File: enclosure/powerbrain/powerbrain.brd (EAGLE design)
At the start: 27.3 x 64.8 mm, 38 parts, among them J2 USB-A-S, J3 AVR_SPI_PRG_6PTH, Q2 200mA/50V, X2 ZX62D-B-5PA8

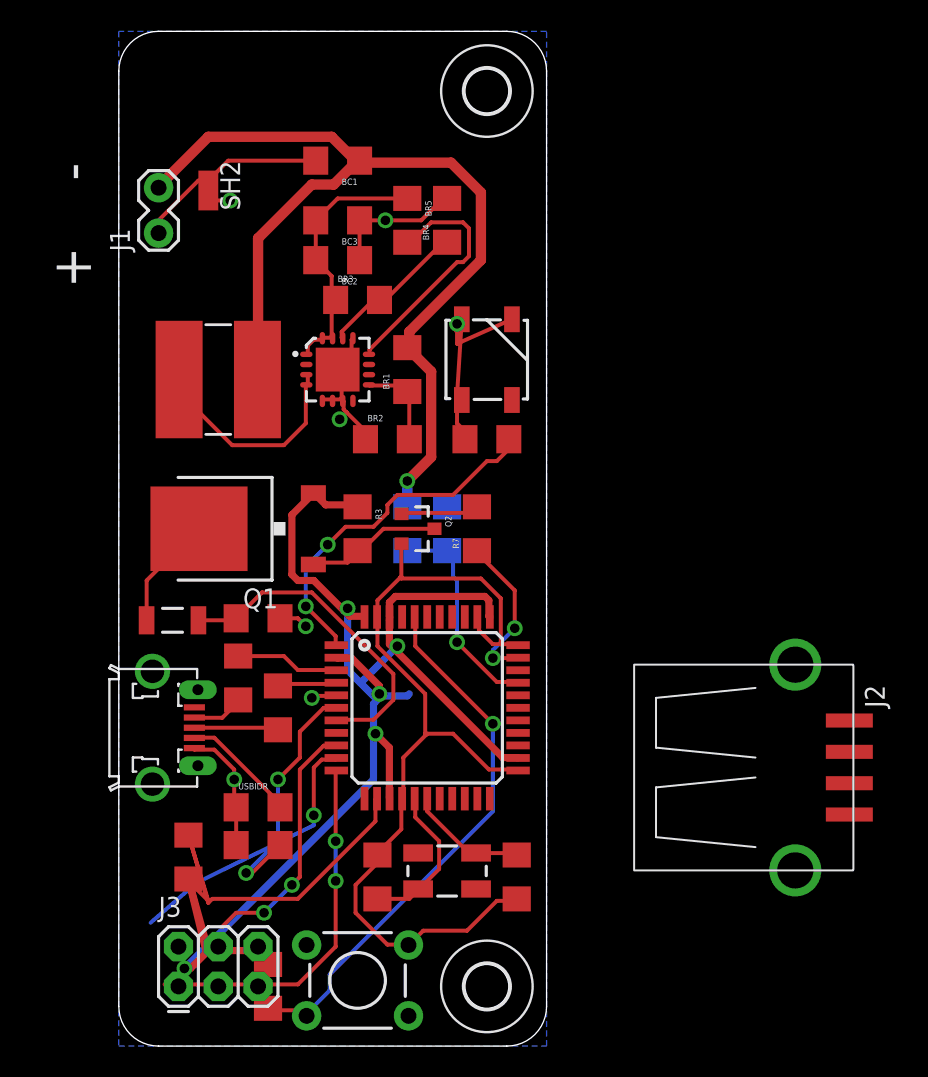
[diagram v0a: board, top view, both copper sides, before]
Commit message: powerbrain: routing improved
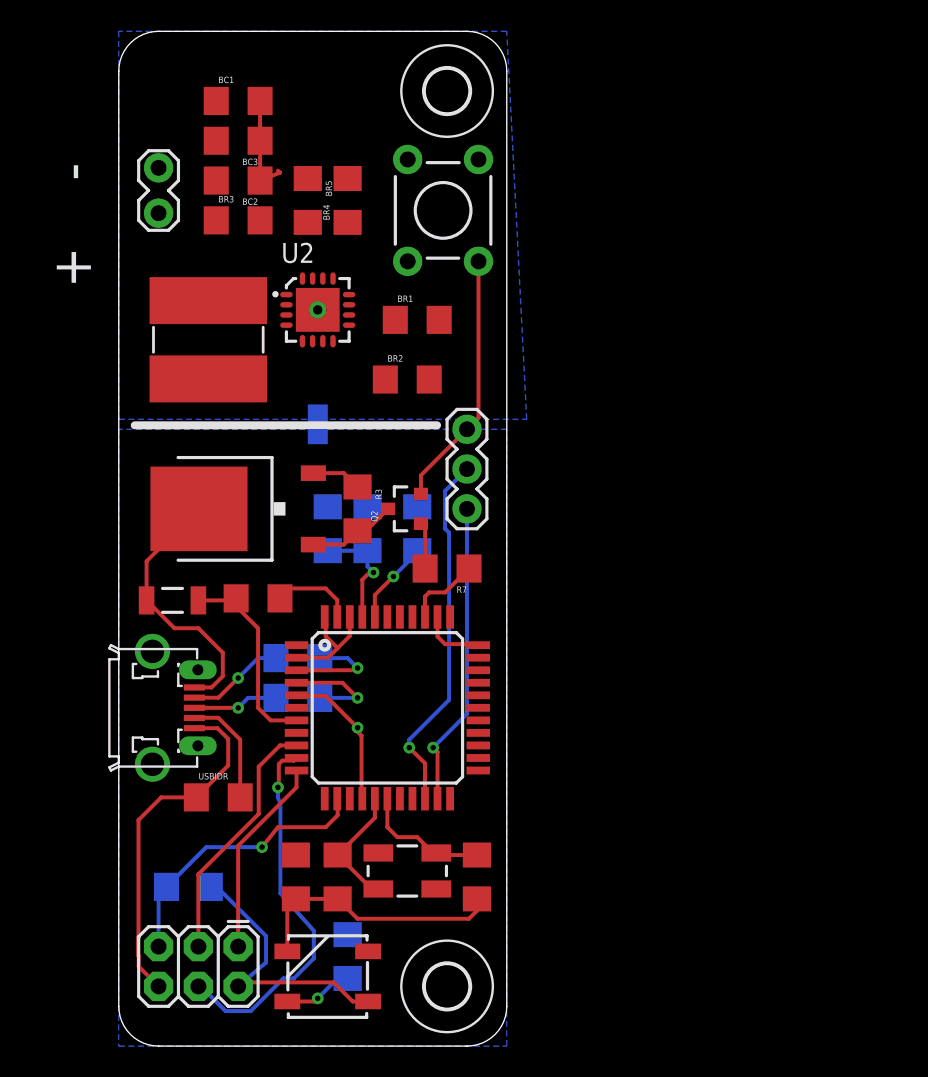
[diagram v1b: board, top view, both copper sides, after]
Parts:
- removed U1: (no value), TPS61090:QFN65P400X400X100-17N
- added U2: TPS61090, TPS61090:QFN65P400X400X100-17N
- J2: value USB-A-S -> (none); device SparkFun-Connectors:USB-A-S -> SparkFun-Connectors:1X03
- J3: value AVR_SPI_PRG_6PTH -> (none)
- moved S1 49.5 mm to (20.7, 53.3), turned to 270 degrees
- moved D2 40.7 mm to (13.3, 4.45), turned to 180 degrees
- moved R_LED 34.2 mm to (14.6, 5.71), flipped to the bottom, turned to 270 degrees
- moved R5 30.7 mm to (19.1, 33.0), flipped to the bottom
- moved J2 26.7 mm to (22.2, 34.3), turned to 90 degrees
- moved SH2 16.5 mm to (12.7, 39.7), flipped to the bottom
- moved BR3 9.16 mm to (7.62, 52.7)
- moved BC2 8.13 mm to (7.62, 55.2)
- moved BC3 8.13 mm to (7.62, 57.8)
- moved BC1 7.41 mm to (7.62, 60.3), turned to 0 degrees
- moved BR5 6.48 mm to (12.1, 54.0)
- moved BR4 6.48 mm to (14.6, 54.0)
- moved VD3 5.08 mm to (13.3, 33.0)
- moved VD4 5.08 mm to (15.9, 33.0)
- moved J3 4.58 mm to (7.62, 6.35), turned to 180 degrees
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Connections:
- removed net N$15: BC2.2, BC3.2, BR3.1, BR5.1, U1.1, U1.15, U1.16
- net BATT_GND: now also BC2.1, BC3.1, BR2.1, BR4.2, U2.13, U2.17, U2.5, U2.6, U2.7, U2.P$1
- net BATT_VCC: now also U2.11, U2.8; no longer U1.11, U1.8
- net B_FB: now also U2.14; no longer U1.14
- net B_LBI: now also U2.9; no longer U1.9
- net B_SW: now also U2.3, U2.4; no longer U1.3, U1.4
- net FOO2: now also U$3.30; no longer U$3.41
- net FOO7: now also U$3.32; no longer U$3.36
- net GND: now also J2.3; no longer BC2.1, BC3.1, BR2.1, BR4.2, U1.13, U1.17, U1.5, U1.6, U1.7
- net N$16: now also U2.12; no longer U1.12
- net PWR_EN: now also U$3.36; no longer U$3.32
- net RX: now also J2.2
- net TX: now also J2.1
- net VCC: now also BC2.2, BC3.2, BR3.1, BR5.1, U2.1, U2.15, U2.16
- net VD_DIRECT: now also U$3.41; no longer U$3.30
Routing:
- net VCC: track 96.2 -> 28.5 mm, vias 5 -> 0
- net BATT_VCC: track 64.2 -> 0.00 mm, vias 1 -> 0
- net BTN: track 35.2 -> 5.35 mm
- net LED: track 23.7 -> 0.00 mm, vias 2 -> 0
- net RX: track 0.00 -> 23.2 mm, vias 0 -> 1
- net GND: track 97.2 -> 75.3 mm, vias 7 -> 1
- net TX: track 0.00 -> 19.5 mm, vias 0 -> 1
- net N$15: track 17.2 -> 0.00 mm
- net N$20: track 16.3 -> 0.00 mm, vias 2 -> 0
- net N$16: track 15.5 -> 0.00 mm
- net B_SW: track 14.1 -> 0.00 mm
- net MISO: track 23.2 -> 12.8 mm, vias 2 -> 0
- net USB_VCC: track 7.25 -> 17.1 mm
- net B_FB: track 9.63 -> 0.00 mm
- net N$22: track 21.2 -> 12.7 mm
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- added copper zone on layer 16, net BATT_GND
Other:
- board size 27.3 x 64.8 mm -> 24.8 x 64.8 mm

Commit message: powerbrain: layout improved
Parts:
- U2: value TPS61090 -> (none)
- moved BR2 22.2 mm to (9.53, 62.9)
- moved C2 19.1 mm to (8.89, 29.7), turned to 180 degrees
- moved S1 14.4 mm to (9.91, 43.8)
- moved BL1 13.3 mm to (18.4, 48.9), turned to 0 degrees
- moved BR1 12.5 mm to (15.9, 58.4), turned to 270 degrees
- moved BC1 11.7 mm to (17.8, 54.6), turned to 180 degrees
- moved BR4 10.2 mm to (5.71, 59.1), turned to 0 degrees
- moved U2 10.2 mm to (11.4, 57.1), turned to 90 degrees
- moved J1 8.64 mm to (5.08, 45.1), turned to 270 degrees
- moved SH2 6.38 mm to (19.1, 40.3)
- moved BC3 6.35 mm to (11.4, 52.7)
- moved BR5 5.85 mm to (6.35, 52.7), turned to 180 degrees
- moved BC2 5.24 mm to (6.35, 50.2), turned to 0 degrees
- moved RRST 4.49 mm to (8.89, 9.53), turned to 270 degrees
- moved BR3 3.70 mm to (5.71, 55.9), turned to 180 degrees
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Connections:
- net BATT_GND: now also U2.10
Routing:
- net BATT_VCC: track 0.00 -> 46.9 mm, vias 0 -> 3
- net VCC: track 28.5 -> 71.2 mm, vias 0 -> 1
- net BATT_GND: track 6.63 -> 35.8 mm
- net N$16: track 0.00 -> 17.8 mm
- net GND: track 75.3 -> 88.4 mm, vias 1 -> 3
- net RST: track 18.0 -> 30.2 mm
- net N$20: track 0.00 -> 10.4 mm
- net B_LBI: track 0.00 -> 8.04 mm
- net B_FB: track 0.00 -> 7.87 mm
- net MOSI: track 23.9 -> 26.7 mm
- net MISO: track 12.8 -> 15.4 mm
- net PWR_EN: track 4.85 -> 3.09 mm
- net N$12: track 2.97 -> 4.19 mm
- net BTN: track 5.35 -> 6.50 mm
- net N$22: track 12.7 -> 11.8 mm
- added copper zone on layer 1, net BATT_GND
- added copper zone on layer 1, net BATT_VCC
- added copper zone on layer 1, net B_SW
- added copper zone on layer 1, net VCC

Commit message: powerbrain: layout improved
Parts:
- added J4: (no value), SparkFun-Connectors:1X02_LOCK
- moved S1 39.6 mm to (12.7, 4.32), turned to 0 degrees
- moved R5 23.9 mm to (10.8, 10.2), turned to 180 degrees
- moved R_LED 23.6 mm to (8.89, 28.6), turned to 0 degrees
- moved D2 12.1 mm to (5.08, 13.3)
- moved USBIDR 6.35 mm to (11.4, 19.7), flipped to the bottom
- moved J3 5.12 mm to (3.81, 8.26), turned to 270 degrees
- moved J1 4.45 mm to (9.53, 45.1)
- moved RRST 4.02 mm to (5.08, 10.8), turned to 180 degrees
- moved BR2 0.93 mm to (10.2, 62.2)
- moved BR3 0.90 mm to (6.35, 55.2)
- moved BR4 0.90 mm to (6.35, 58.4)
- moved BL1 0.64 mm to (18.4, 48.3)
- moved BR1 0.64 mm to (15.9, 57.8)
- moved C5 0.63 mm to (14.0, 10.2)
- moved BC1 0.63 mm to (17.8, 54.0)
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- renumbered VD3 to VD1, VD4 to VD2
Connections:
- net BATT_GND: now also J4.1
- net BATT_VCC: now also J4.2
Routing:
- net BTN: track 6.50 -> 35.3 mm
- net N$7: track 4.46 -> 27.6 mm
- net VCC: track 71.2 -> 92.5 mm, vias 1 -> 2
- net GND: track 88.4 -> 75.7 mm, vias 3 -> 2
- net MOSI: track 26.7 -> 17.3 mm
- net TX: track 19.5 -> 24.6 mm
- net RST: track 30.2 -> 25.8 mm
- net LED: track 0.00 -> 4.31 mm, vias 0 -> 1
- net SCK: track 16.2 -> 20.3 mm
- net N$12: track 4.19 -> 6.30 mm
- net N$16: track 17.8 -> 16.3 mm
- net MISO: track 15.4 -> 13.9 mm
- net N$1: track 7.19 -> 5.72 mm, vias 0 -> 1
- net BATT_VCC: track 46.9 -> 47.9 mm
- net USB_VCC: track 17.6 -> 18.3 mm
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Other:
- board text added: "1"
- board text added: "2"
- board text added: "G"
- board text added: "ID"

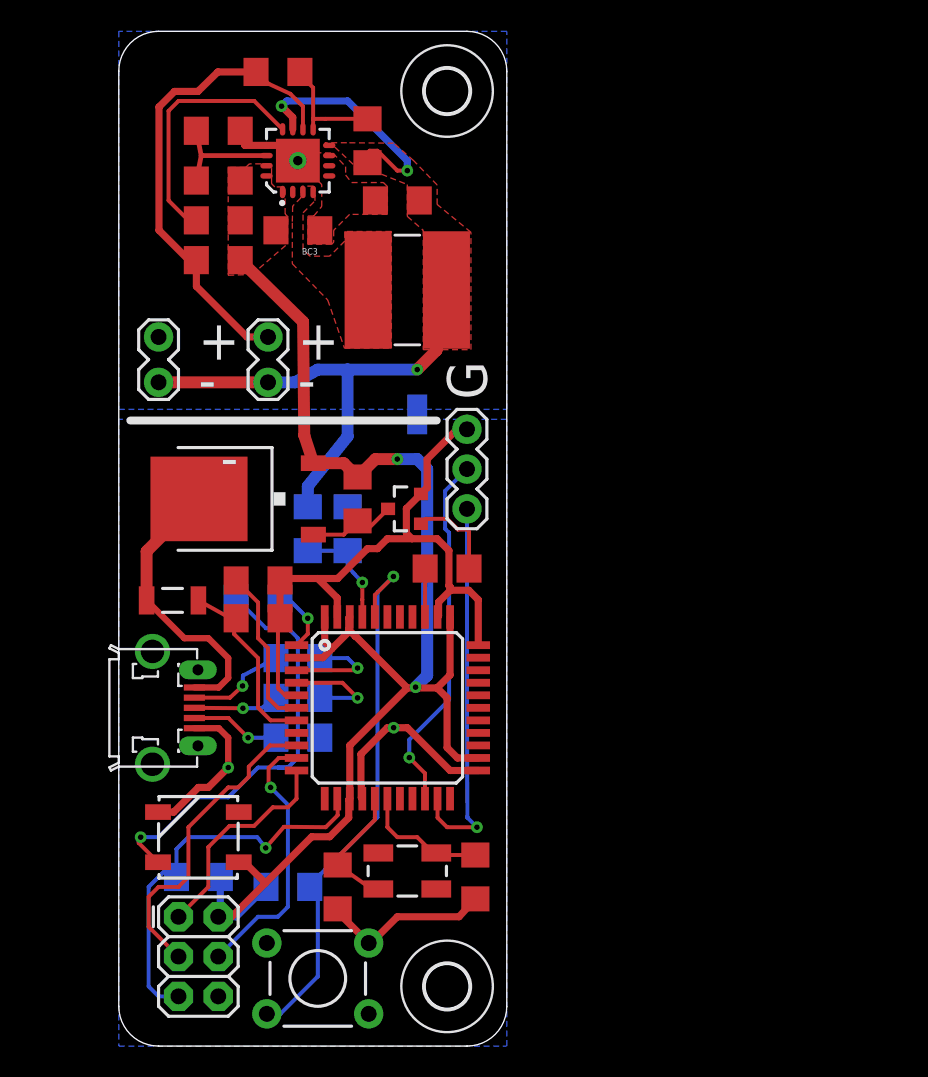
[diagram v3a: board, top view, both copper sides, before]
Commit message: powerbrain: USB OTG vbus unclear
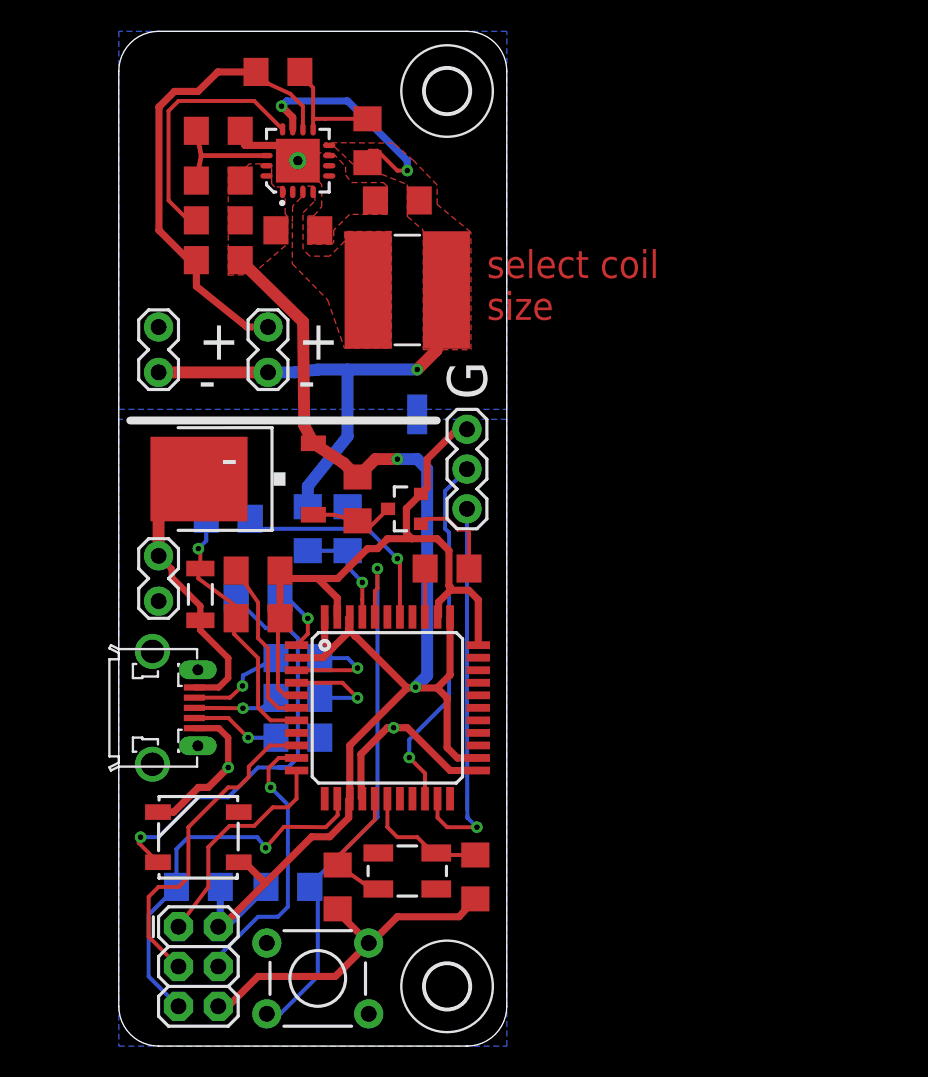
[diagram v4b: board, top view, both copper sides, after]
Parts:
- added J5: (no value), SparkFun-Connectors:1X02_LOCK
- added RUSB3: (no value), SparkFun-Passives:1206
- moved F2 1.82 mm to (5.21, 28.8), turned to 90 degrees
- moved Q1 1.27 mm to (7.62, 36.2)
- moved C2 0.64 mm to (8.89, 30.4)
- moved J3 0.64 mm to (3.81, 7.62)
- moved RRST 0.63 mm to (5.08, 10.2)
- moved J1 0.63 mm to (9.53, 45.7)
- moved J4 0.63 mm to (2.54, 45.7)
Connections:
- removed net FOO1: U$3.38
- removed net N$22: C3.1, F2.2, U$3.7
- new net $N23: C3.1, F2.2, RUSB3.1, U$3.7
- new net VBUS_SENSE: RUSB3.2, U$3.38
- net GND: now also J5.1
- net USB_VCC: now also J5.2
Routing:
- net $N23: track 0.00 -> 17.1 mm, vias 0 -> 1
- net VBUS_SENSE: track 0.00 -> 14.2 mm, vias 0 -> 1
- net GND: track 75.7 -> 88.0 mm
- net N$22: track 11.8 -> 0.00 mm
- net RST: track 25.8 -> 24.5 mm
- net SCK: track 20.3 -> 20.9 mm
- net MOSI: track 17.3 -> 17.9 mm
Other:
- board text added: "select coil size"

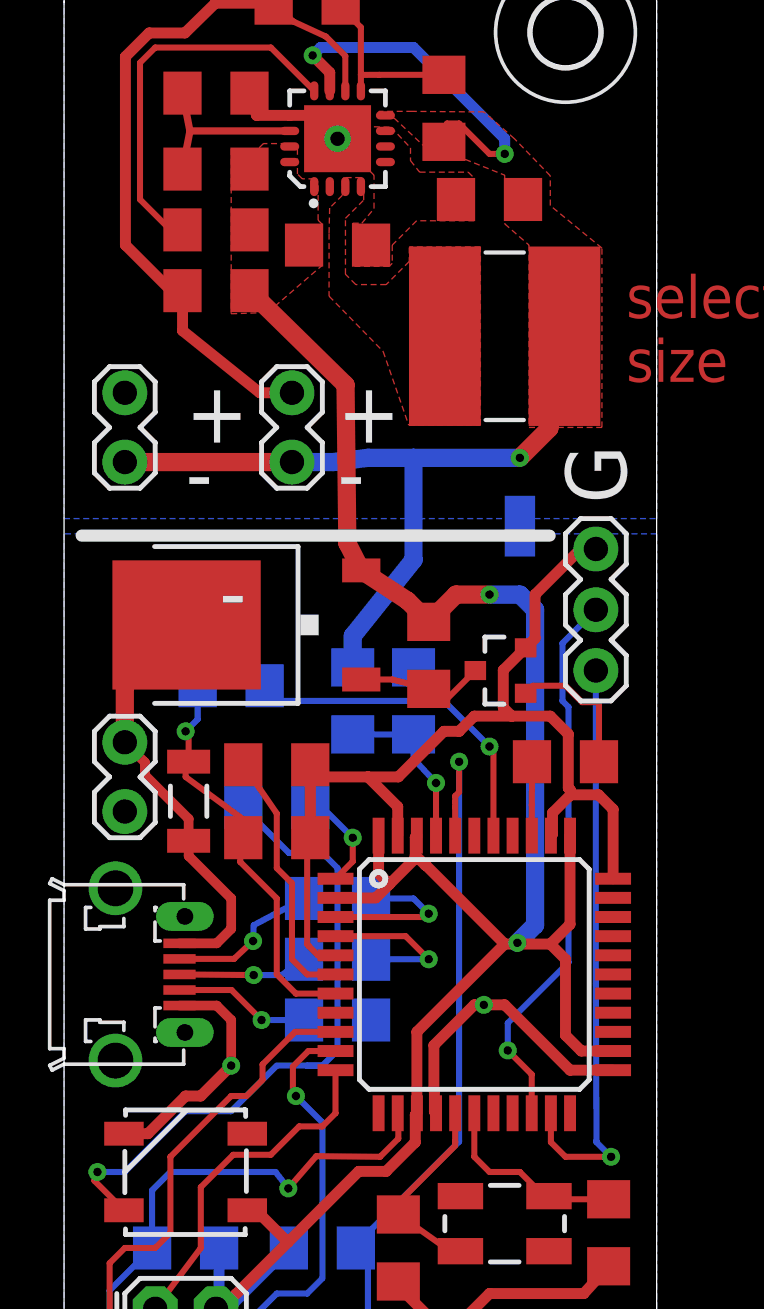
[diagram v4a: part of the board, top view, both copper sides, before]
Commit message: powerbrain: VBUS switch
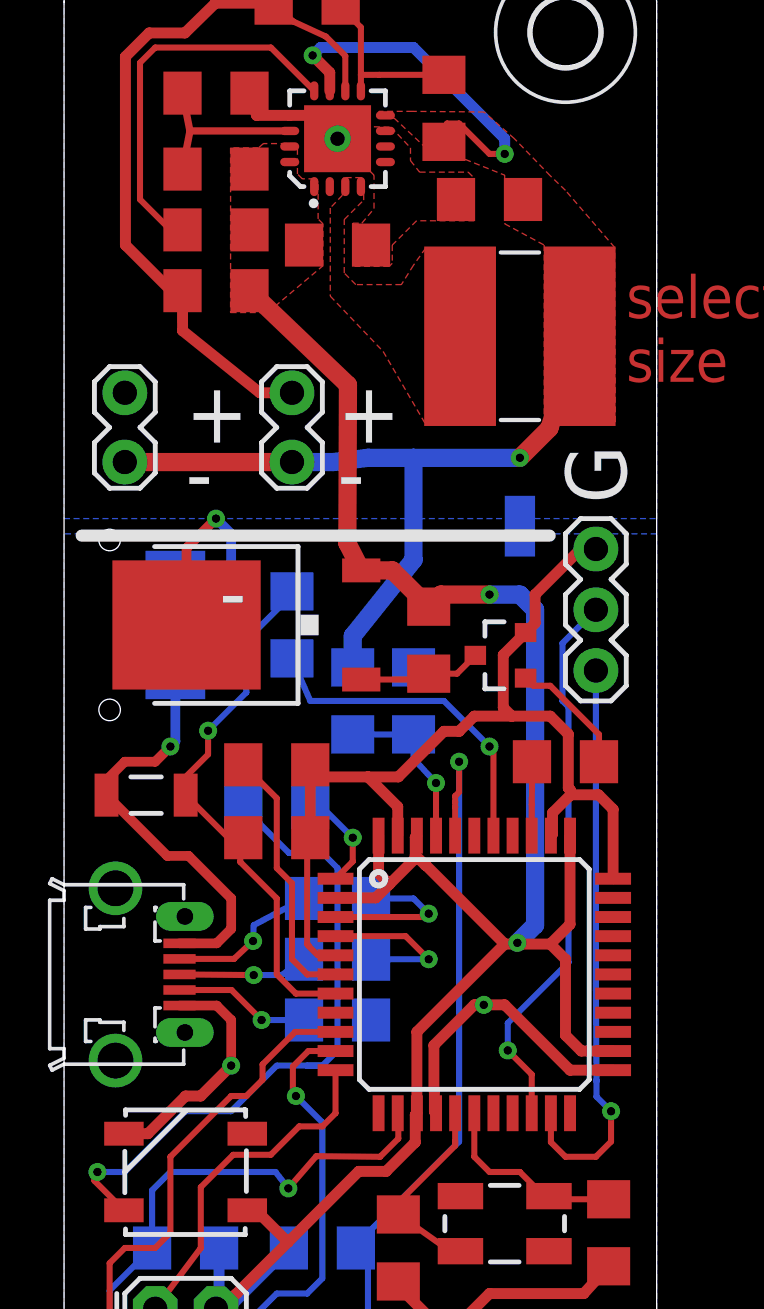
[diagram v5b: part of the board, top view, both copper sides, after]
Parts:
- removed J5: (no value), SparkFun-Connectors:1X02_LOCK
- added S2: (no value), SparkFun-Electromechanical:SWITCH-SPDT-SMD
- moved RUSB3 3.59 mm to (9.53, 36.2), turned to 270 degrees
- moved F2 1.80 mm to (3.43, 29.1), turned to 0 degrees
- moved R3 0.64 mm to (15.2, 35.6)
- moved BL1 0.64 mm to (19.1, 48.3)
- moved Q2 0.63 mm to (18.3, 34.9)
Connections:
- new net USB_VCC_OUT: F2.1, S2.3, X2.1
- net GND: no longer J5.1
- net USB_VCC: now also S2.2; no longer F2.1, J5.2, X2.1
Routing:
- net USB_VCC_OUT: track 0.00 -> 17.2 mm, vias 0 -> 1
- net USB_VCC: track 18.0 -> 11.6 mm, vias 0 -> 1
- net $N23: track 17.1 -> 22.7 mm
- net N$12: track 6.30 -> 5.18 mm
- net N$6: track 5.69 -> 5.19 mm
